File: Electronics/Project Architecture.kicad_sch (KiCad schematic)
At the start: 33 parts, among them U1 TMP102xxDRL

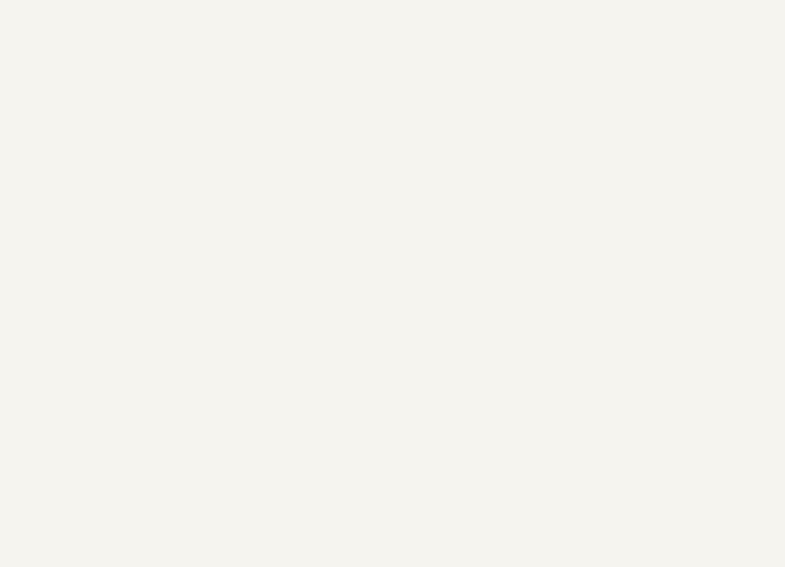
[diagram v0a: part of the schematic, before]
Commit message: RP2040 Added, Files Structure Changed
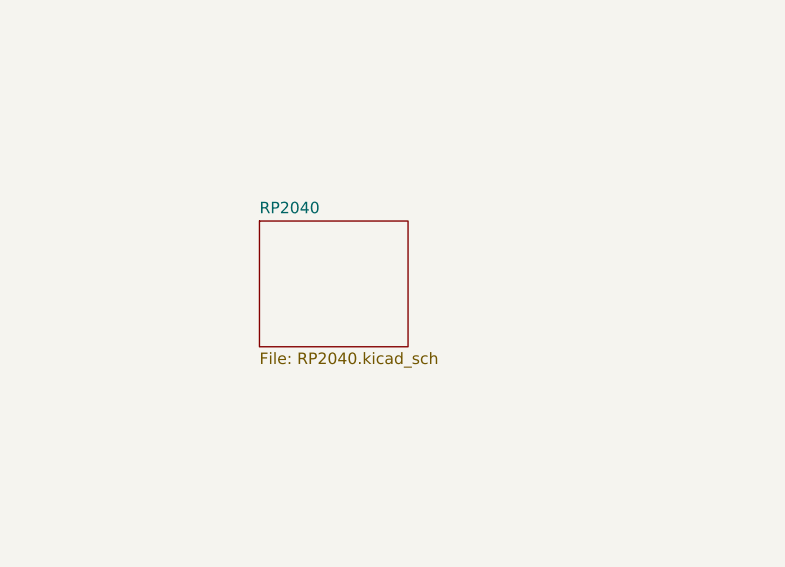
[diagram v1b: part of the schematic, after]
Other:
- added sheet RP2040 (RP2040.kicad_sch)
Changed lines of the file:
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@@
 			(project "CM5 Nas"
 				(path "/0650c7a8-acba-429c-9f8e-eec0baf0bc1c/fede4c36-00cc-4d3d-b71c-5243ba232202"
-					(page "7")
+					(page "8")
 				)
 			)
@@
 			(project "CM5 Nas"
 				(path "/0650c7a8-acba-429c-9f8e-eec0baf0bc1c/fede4c36-00cc-4d3d-b71c-5243ba232202"
-					(page "9")
+					(page "10")
 				)
 			)
@@
 			(project "CM5 Nas"
 				(path "/0650c7a8-acba-429c-9f8e-eec0baf0bc1c/fede4c36-00cc-4d3d-b71c-5243ba232202"
-					(page "6")
+					(page "7")
 				)
 			)
@@
 			(project "CM5 Nas"
 				(path "/0650c7a8-acba-429c-9f8e-eec0baf0bc1c/fede4c36-00cc-4d3d-b71c-5243ba232202"
-					(page "10")
+					(page "11")
 				)
 			)
@@
 	)
 	(sheet
+		(at 38.1 156.21)
+		(size 16.51 13.97)
+		(exclude_from_sim no)
+		(in_bom yes)
+		(on_board yes)
+		(dnp no)
+		(fields_autoplaced yes)
+		(stroke
+			(width 0.1524)
+			(type solid)
+		)
+		(fill
+			(color 0 0 0 0.0000)
+		)
+		(property "Sheetname" "RP2040"
+			(at 38.1 155.4984 0)
+			(effects
+				(font
+					(size 1.27 1.27)
+				)
+				(justify left bottom)
+			)
+		)
+		(property "Sheetfile" "RP2040.kicad_sch"
+			(at 38.1 170.7646 0)
+			(effects
+				(font
+					(size 1.27 1.27)
+				)
+				(justify left top)
+			)
+		)
+		(instances
+			(project "CM5 Nas"
+				(path "/0650c7a8-acba-429c-9f8e-eec0baf0bc1c/fede4c36-00cc-4d3d-b71c-5243ba232202"
+					(page "12")
+				)
+			)
+		)
+	)
+	(sheet
 		(at 241.3 101.6)
 		(size 25.4 25.4)
@@
 			(project "CM5 Nas"
 				(path "/0650c7a8-acba-429c-9f8e-eec0baf0bc1c/fede4c36-00cc-4d3d-b71c-5243ba232202"
-					(page "8")
-				)
-			)
+					(page "9")
+				)
+			)

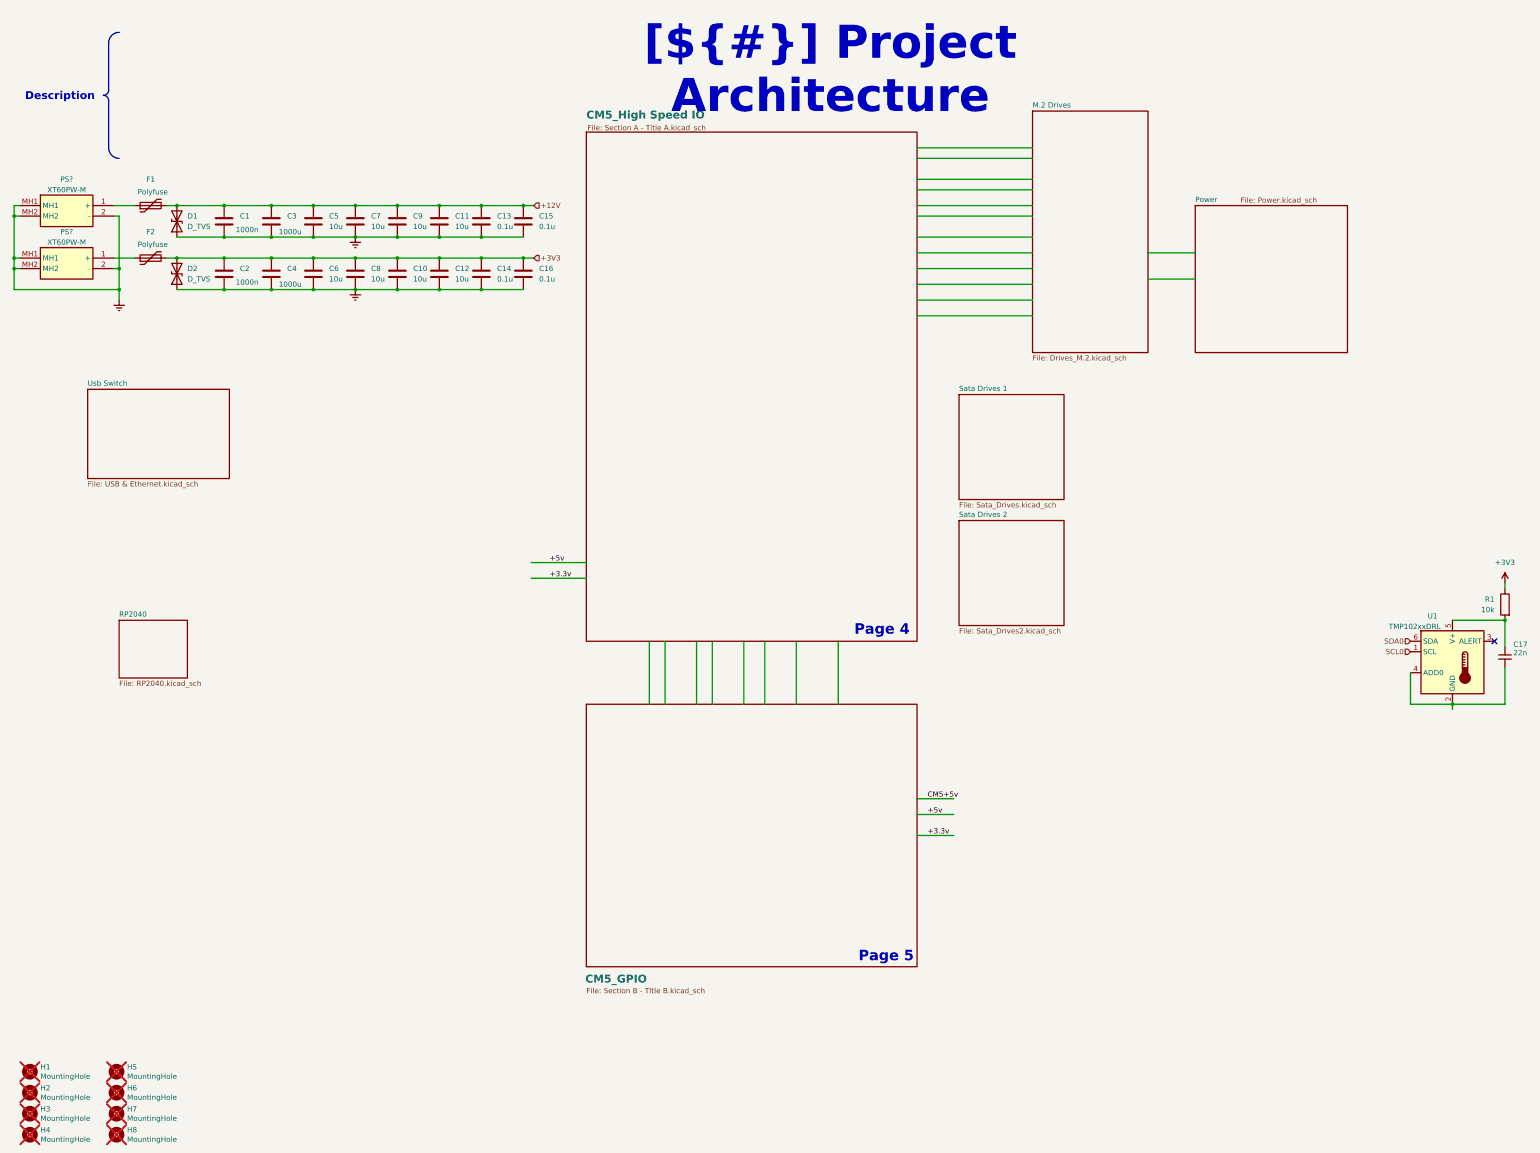
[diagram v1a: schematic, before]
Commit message: Rp2040 Power Sequence finished and general cleaning
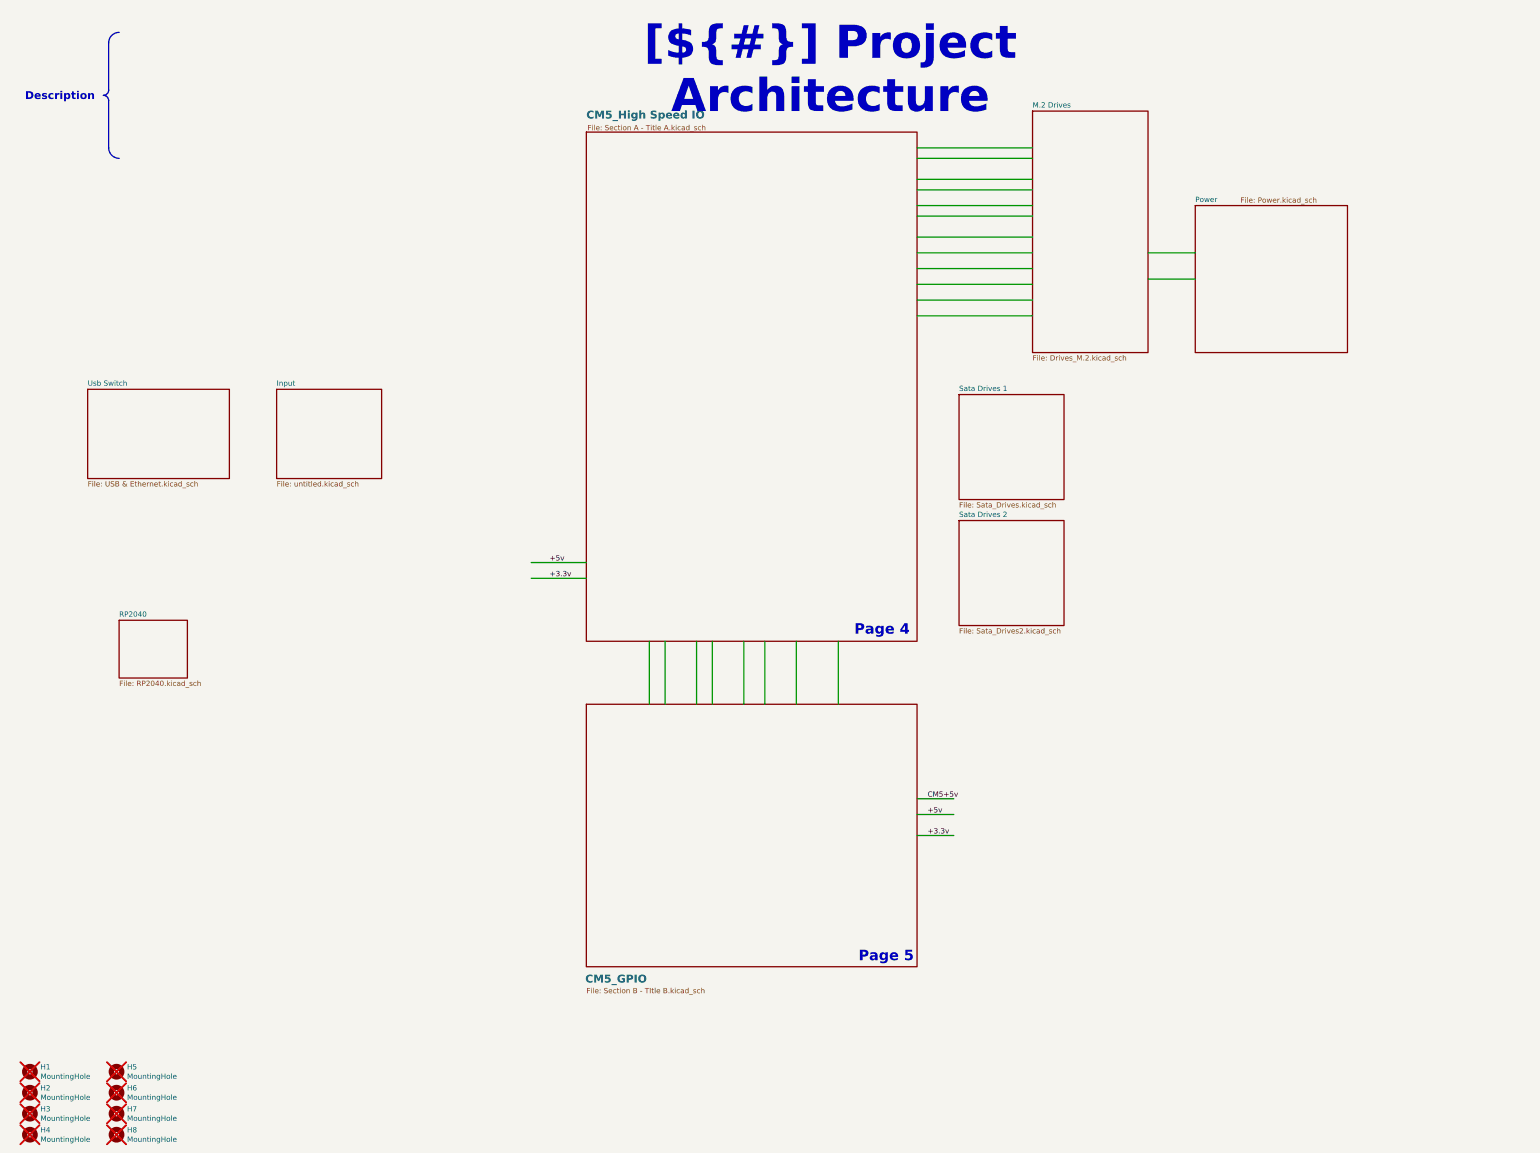
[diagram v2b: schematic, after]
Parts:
- removed C1, C2: 1000n, symbol Device:C
- removed C10, C11, C12, C5, C6, C7, C8, C9: 10u, symbol Device:C
- removed C13, C14, C15, C16: 0.1u, symbol Device:C
- removed C17: 22n, symbol Device:C_Small
- removed C3, C4: 1000u, symbol Device:C
- removed D1, D2: D_TVS, symbol Device:D_TVS
- removed F1, F2: Polyfuse, symbol Device:Polyfuse
- removed PS? (x2): XT60PW-M, XT60PWM, symbol XT60PW-M:XT60PW-M
- removed R1: 10k, symbol Device:R
- removed U1: TMP102xxDRL, Package_TO_SOT_SMD:SOT-563, symbol Sensor_Temperature:TMP102xxDRL
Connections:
- no-connect marks 1 -> 0
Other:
- added sheet Input (untitled.kicad_sch)

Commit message: Starting the Sheet connections
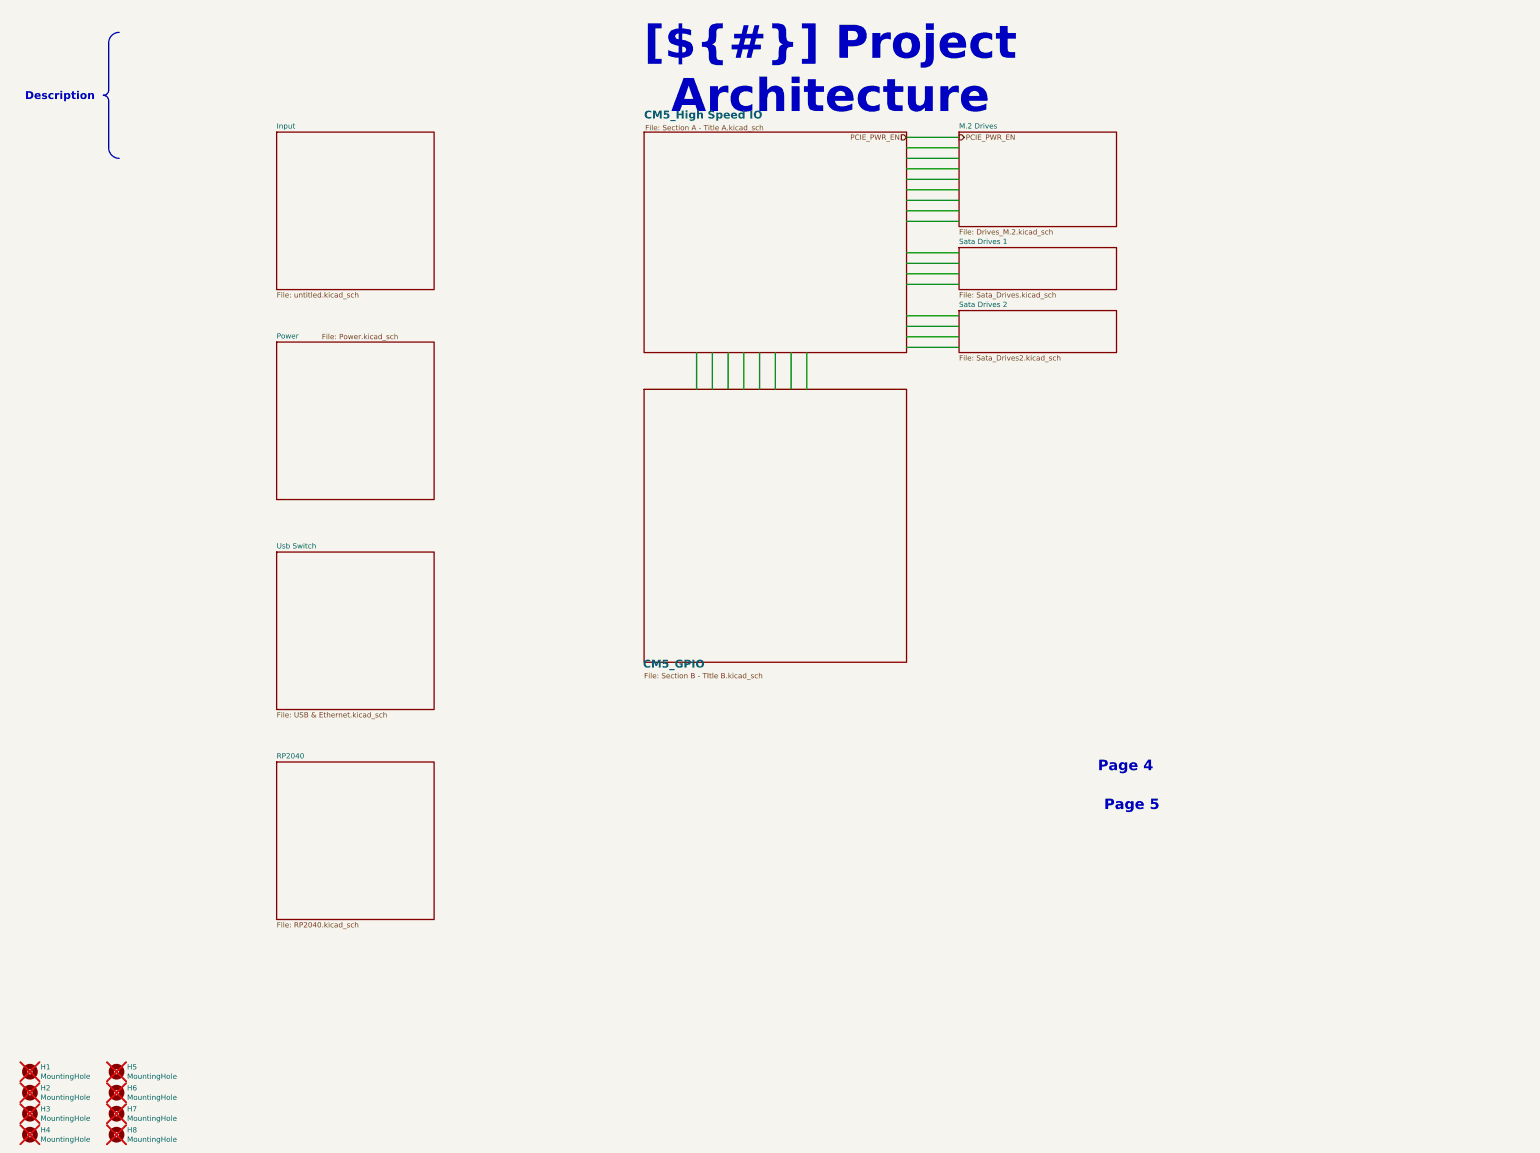
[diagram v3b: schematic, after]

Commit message: Footprints Selected
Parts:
- H1, H2, H3, H4, H5, H6, H7, H8: footprint CM5IO:MountingHole_2.7mm_M2.5_DIN965 -> MountingHole:MountingHole_2.7mm_M2.5_DIN965

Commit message: Footprints selected, Hiracicle connections created, Pcb next
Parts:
- H1, H8: footprint MountingHole:MountingHole_2.7mm_M2.5_DIN965 -> MountingHole:MountingHole_2.7mm_M2.5
- H2: renamed from H5; footprint MountingHole:MountingHole_2.7mm_M2.5_DIN965 -> MountingHole:MountingHole_2.7mm_M2.5
- H3: renamed from H2; footprint MountingHole:MountingHole_2.7mm_M2.5_DIN965 -> MountingHole:MountingHole_2.7mm_M2.5
- H4: renamed from H6; footprint MountingHole:MountingHole_2.7mm_M2.5_DIN965 -> MountingHole:MountingHole_2.7mm_M2.5
- H5: renamed from H3; footprint MountingHole:MountingHole_2.7mm_M2.5_DIN965 -> MountingHole:MountingHole_2.7mm_M2.5
- H6: renamed from H7; footprint MountingHole:MountingHole_2.7mm_M2.5_DIN965 -> MountingHole:MountingHole_2.7mm_M2.5
- H7: renamed from H4; footprint MountingHole:MountingHole_2.7mm_M2.5_DIN965 -> MountingHole:MountingHole_2.7mm_M2.5
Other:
- removed sheet RP2040
- note removed: "Page 4"
- note removed: "Page 5"
